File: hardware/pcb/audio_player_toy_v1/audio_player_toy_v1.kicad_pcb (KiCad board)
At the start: 2 copper layers, 70 x 50 mm, 14 parts, among them J1 Conn_02x05_Odd_Even, U1 ISD2360YYI, U2 BH-AAA-B5AA005

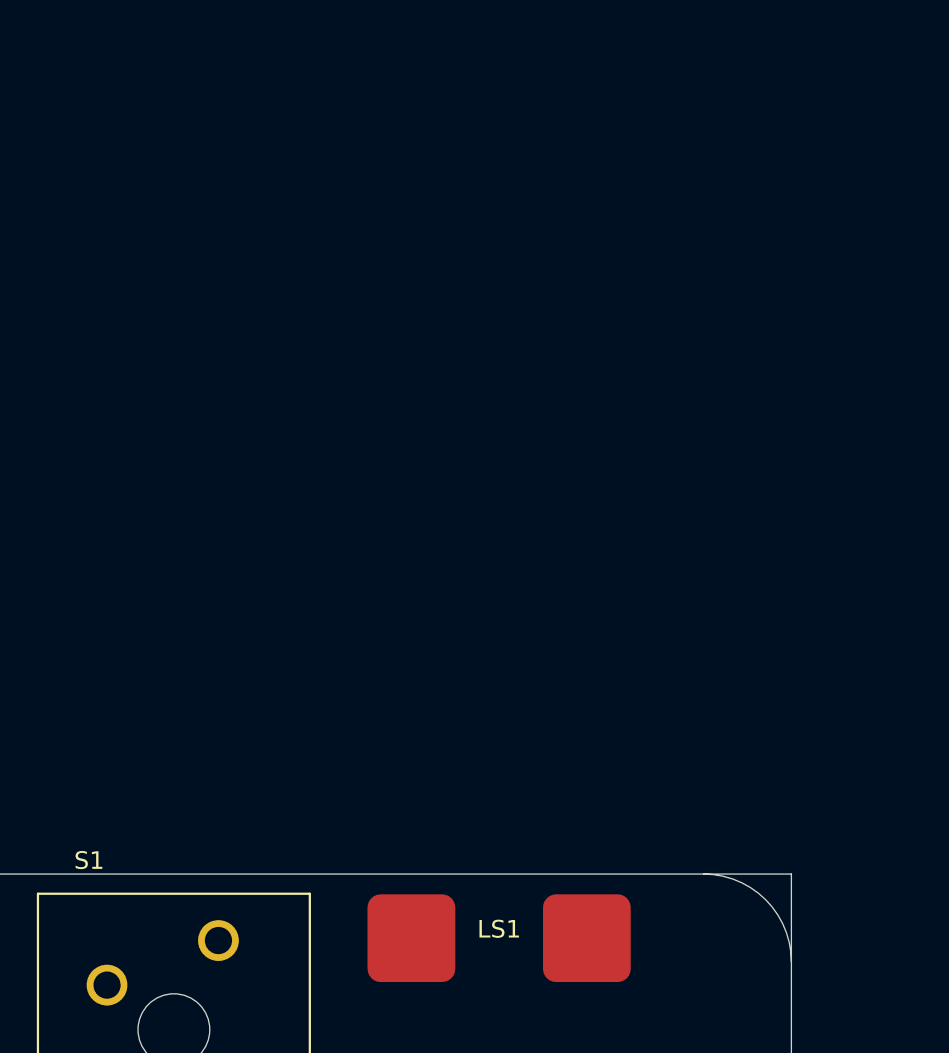
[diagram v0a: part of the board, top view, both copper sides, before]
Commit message: feat: add TH speaker capacbility
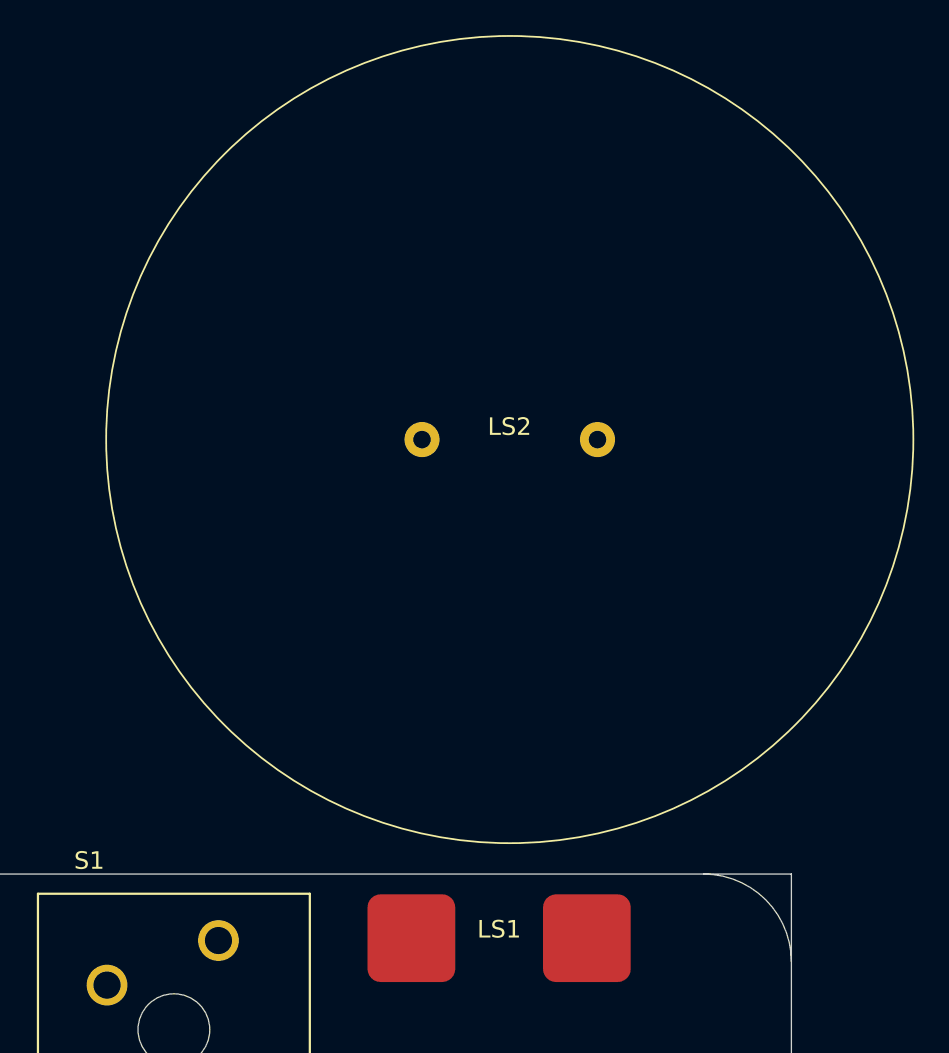
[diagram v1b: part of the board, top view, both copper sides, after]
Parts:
- added LS2: Speaker, .pretty:Speaker_TH, F.Cu at (153.9, 75.2)
- LS1: footprint .pretty:Speaker -> .pretty:Speaker_SMD
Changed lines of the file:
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@@
 		)
 	)
-	(footprint ".pretty:Speaker"
+	(footprint ".pretty:Speaker_SMD"
 		(layer "F.Cu")
 		(at 153.345 103.655)
 		(property "Reference" "LS1"
-			(at 0 -0.499999 0)
+			(at 0 -0.5 0)
 			(unlocked yes)
 			(layer "F.SilkS")
@@
 			(solder_mask_margin 0.102)
 		)
+		(embedded_fonts no)
+	)
+	(footprint ".pretty:Speaker_TH"
+		(layer "F.Cu")
+		(at 153.95 75.24)
+		(property "Reference" "LS2"
+			(at -0.01 -0.73 0)
+			(unlocked yes)
+			(layer "F.SilkS")
+			(effects
+				(font
+					(size 1 1)
+					(thickness 0.1)
+				)
+			)
+		)
+		(property "Value" "Speaker"
+			(at 0 1 0)
+			(unlocked yes)
+			(layer "F.Fab")
+			(effects
+				(font
+					(size 1 1)
+					(thickness 0.15)
+				)
+			)
+		)
+		(property "Datasheet" "~"
+			(at 0 0 0)
+			(unlocked yes)
+			(layer "F.Fab")
+			(hide yes)
+			(effects
+				(font
+					(size 1 1)
+					(thickness 0.15)
+				)
+			)
+		)
+		(property "Description" "Speaker"
+			(at 0 0 0)
+			(unlocked yes)
+			(layer "F.Fab")
+			(hide yes)
+			(effects
+				(font
+					(size 1 1)
+					(thickness 0.15)
+				)
+			)
+		)
+		(sheetname "/")
+		(sheetfile "audio_player_toy_v1.kicad_sch")
+		(attr smd)
+		(fp_circle
+			(center 0 0)
+			(end 23 0)
+			(stroke
+				(width 0.1)
+				(type solid)
+			)
+			(fill no)
+			(layer "F.SilkS")
+		)
+		(fp_circle
+			(center 0 0)
+			(end 23.5 0)
+			(stroke
+				(width 0.1)
+				(type solid)
+			)
+			(fill no)
+			(layer "F.CrtYd")
+		)
+		(fp_text user "${REFERENCE}"
+			(at 0 2.5 0)
+			(unlocked yes)
+			(layer "F.Fab")
+			(effects
+				(font
+					(size 1 1)
+					(thickness 0.15)
+				)
+			)
+		)
+		(pad "1" thru_hole circle
+			(at -5 0)
+			(size 2 2)
+			(drill 1)
+			(layers "*.Cu" "*.Mask")
+			(remove_unused_layers no)
+			(net 23 "SPK+")
+			(pinfunction "1")
+			(pintype "input")
+			(solder_mask_margin 0.102)
+		)
+		(pad "2" thru_hole circle
+			(at 5 0)
+			(size 2 2)
+			(drill 1)
+			(layers "*.Cu" "*.Mask")
+			(remove_unused_layers no)
+			(net 29 "SPK-")
+			(pinfunction "2")
+			(pintype "input")
+			(solder_mask_margin 0.102)
+		)

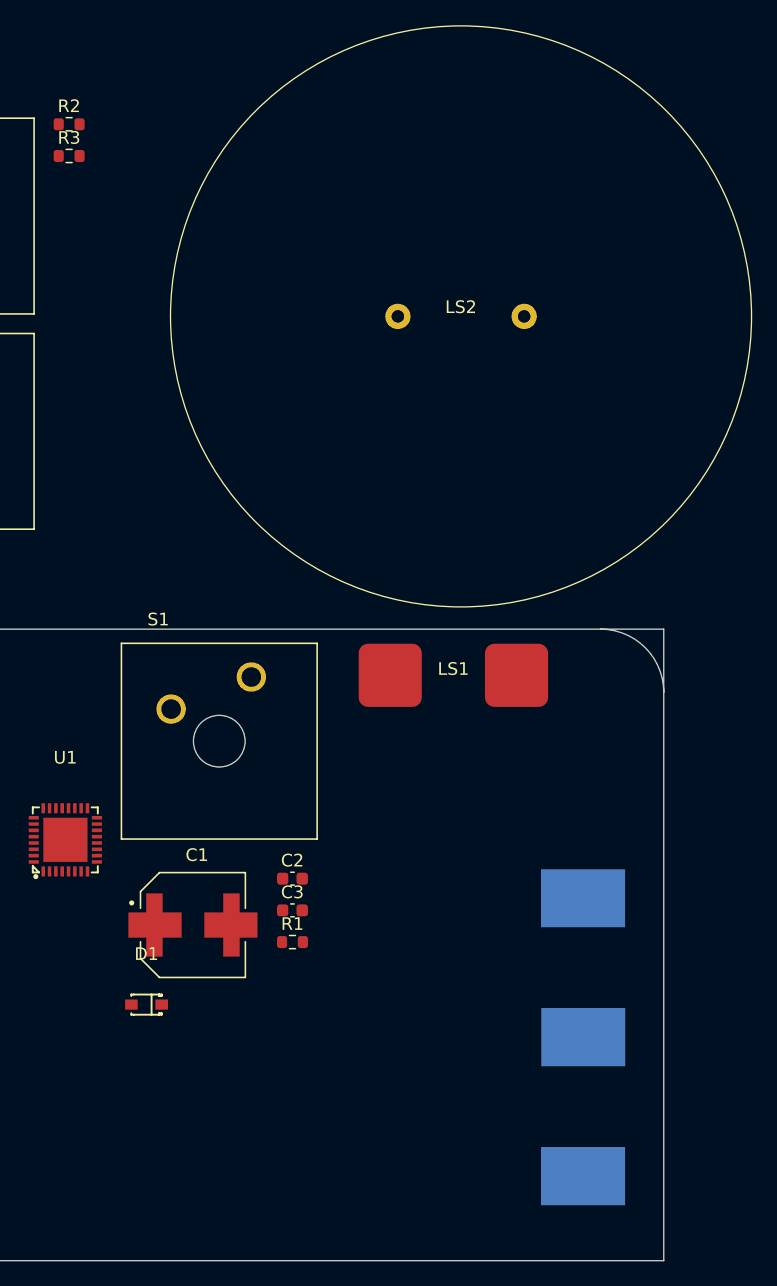
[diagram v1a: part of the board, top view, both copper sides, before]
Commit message: chore: update footprint of speaker TH
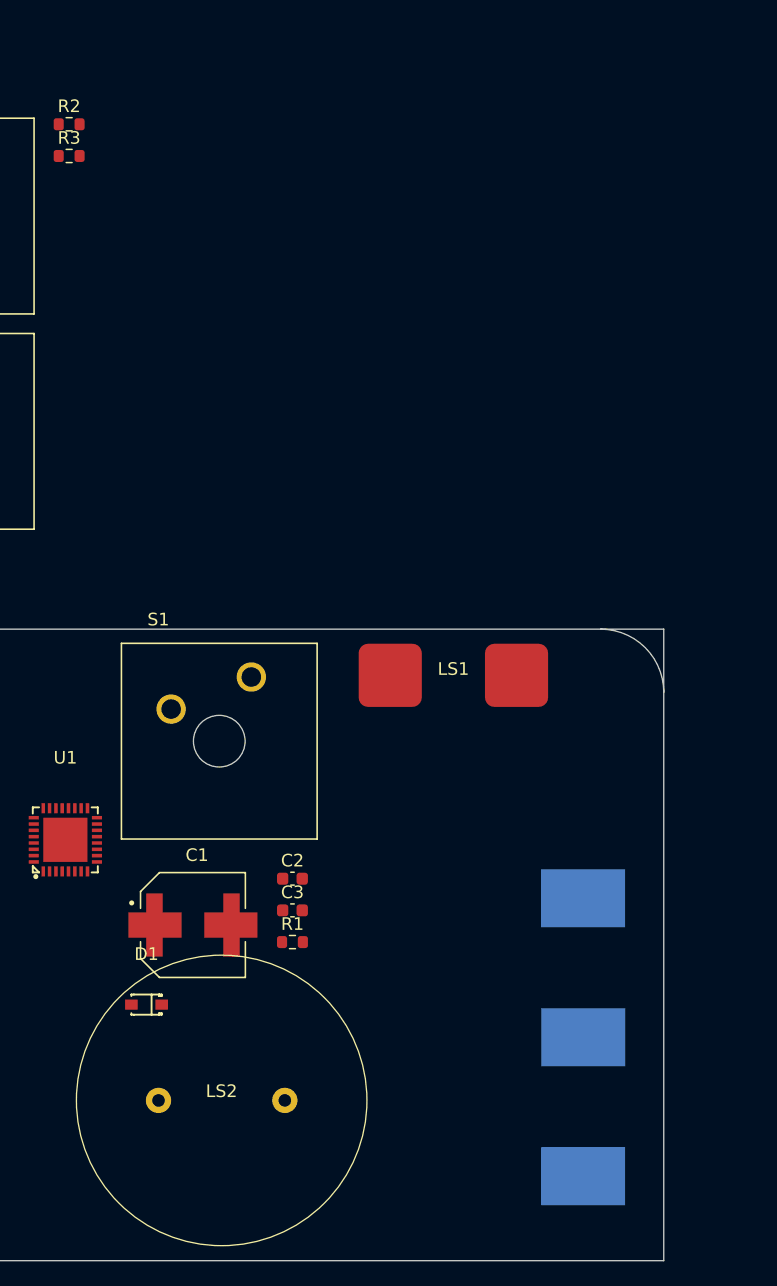
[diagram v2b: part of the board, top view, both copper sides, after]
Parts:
- moved LS2 64.9 mm to (135.0, 137.3)
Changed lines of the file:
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@@
 	(footprint ".pretty:Speaker_TH"
 		(layer "F.Cu")
-		(at 153.95 75.24)
+		(at 135 137.31)
 		(property "Reference" "LS2"
 			(at -0.01 -0.73 0)
@@
 		(fp_circle
 			(center 0 0)
-			(end 23 0)
+			(end 11.5 0)
 			(stroke
 				(width 0.1)
@@
 		(fp_circle
 			(center 0 0)
-			(end 23.5 0)
+			(end 12 0)
 			(stroke
 				(width 0.1)

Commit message: chore: finalize the location of main component
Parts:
- moved D1 60.2 mm to (79.2, 96.0)
- moved U1 60.2 mm to (72.8, 82.9)
- moved R1 60.2 mm to (90.8, 91.0)
- moved C1 60.2 mm to (82.9, 89.7)
- moved C2 60.2 mm to (90.8, 86.0)
- moved C3 60.2 mm to (90.8, 88.5)
- moved S2 50.5 mm to (135.0, 112.5)
- moved J1 37.7 mm to (135.2, 80.9)
- moved S3 28.3 mm to (115.0, 112.5)
- moved S1 20.5 mm to (155.0, 112.5)
- moved LS1 16.1 mm to (153.0, 87.5)
- moved U2 0.76 mm to (135.0, 132.0)
- moved LS2 0.63 mm to (135.0, 136.7)
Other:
- board size 70 x 50 mm -> 70 x 52.5 mm
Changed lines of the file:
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@@
 	(footprint "Capacitor_SMD:C_0603_1608Metric"
 		(layer "F.Cu")
-		(at 140.605 119.755)
+		(at 90.795 85.985)
 		(descr "Capacitor SMD 0603 (1608 Metric), square (rectangular) end terminal, IPC-7351 nominal, (Body size source: IPC-SM-782 page 76, https://www.pcb-3d.com/wordpress/wp-content/uploads/ipc-sm-782a_amendment_1_and_2.pdf), generated with kicad-footprint-generator")
 		(tags "capacitor")
@@
 	(footprint ".pretty:SOD-323_L1.8-W1.3-LS2.5-FD"
 		(layer "F.Cu")
-		(at 129.05 129.725)
+		(at 79.24 95.955)
 		(property "Reference" "D1"
 			(at 0 -4 0)
@@
 	(footprint "Capacitor_SMD:C_0603_1608Metric"
 		(layer "F.Cu")
-		(at 140.605 122.265)
+		(at 90.795 88.495)
 		(descr "Capacitor SMD 0603 (1608 Metric), square (rectangular) end terminal, IPC-7351 nominal, (Body size source: IPC-SM-782 page 76, https://www.pcb-3d.com/wordpress/wp-content/uploads/ipc-sm-782a_amendment_1_and_2.pdf), generated with kicad-footprint-generator")
 		(tags "capacitor")
@@
 	(footprint ".pretty:Speaker_SMD"
 		(layer "F.Cu")
-		(at 153.345 103.655)
+		(at 153 87.54)
 		(property "Reference" "LS1"
 			(at 0 -0.5 0)
@@
 	(footprint ".pretty:SW_MX1A-11NN"
 		(layer "F.Cu")
-		(at 134.81 108.87)
+		(at 155 112.5)
 		(property "Reference" "S1"
 			(at -4.822 -9.632 0)
@@
 	(footprint "Resistor_SMD:R_0603_1608Metric"
 		(layer "F.Cu")
-		(at 140.605 124.775)
+		(at 90.795 91.005)
 		(descr "Resistor SMD 0603 (1608 Metric), square (rectangular) end terminal, IPC-7351 nominal, (Body size source: IPC-SM-782 page 72, https://www.pcb-3d.com/wordpress/wp-content/uploads/ipc-sm-782a_amendment_1_and_2.pdf), generated with kicad-footprint-generator")
 		(tags "resistor")
@@
 	(footprint ".pretty:SW_MX1A-11NN"
 		(layer "F.Cu")
-		(at 112.4 67.296)
+		(at 135 112.5)
 		(property "Reference" "S2"
 			(at -4.822 -9.632 0)
@@
 	(footprint ".pretty:Speaker_TH"
 		(layer "F.Cu")
-		(at 135 137.31)
+		(at 135 136.675)
 		(property "Reference" "LS2"
 			(at -0.01 -0.73 0)
@@
 	(footprint ".pretty:CAP_EEEFK1A221V"
 		(layer "F.Cu")
-		(at 132.725 123.425)
+		(at 82.915 89.655)
 		(property "Reference" "C1"
 			(at 0.325 -5.535 0)
@@
 	(footprint ".pretty:TQFN-32_L5.0-W5.0-P0.50-BL-EP3.5"
 		(layer "F.Cu")
-		(at 122.625 116.68)
+		(at 72.815 82.91)
 		(property "Reference" "U1"
 			(at 0 -6.5 0)
@@
 	(footprint "Connector_PinHeader_2.54mm:PinHeader_2x05_P2.54mm_Vertical"
 		(layer "F.Cu")
-		(at 105.635 104.26)
+		(at 135.215 80.93)
 		(descr "Through hole straight pin header, 2x05, 2.54mm pitch, double rows")
 		(tags "Through hole pin header THT 2x05 2.54mm double row")
@@
 	(footprint ".pretty:SW_MX1A-11NN"
 		(layer "F.Cu")
-		(at 112.4 84.34)
+		(at 115 112.5)
 		(property "Reference" "S3"
 			(at -4.822 -9.632 0)
@@
 	(footprint ".pretty:BAT-SMD_BH-AAA-B5AA005"
 		(layer "B.Cu")
-		(at 135.695 132.305 180)
+		(at 135 132 180)
 		(property "Reference" "U2"
 			(at 0 15 0)
@@
 		)
 	)
-	(gr_arc
-		(start 165 100)
-		(mid 168.535534 101.464466)
-		(end 170 105)
+	(gr_rect
+		(start 117.42 131.175)
+		(end 152.42 142.175)
 		(stroke
-			(width 0.05)
-			(type default)
+			(width 0.1)
+			(type solid)
 		)
-		(layer "Edge.Cuts")
+		(fill no)
+		(layer "F.SilkS")
 	)
 	(gr_rect
 		(start 100 100)
-		(end 170 150)
+		(end 170 152.5)
 		(stroke
 			(width 0.05)

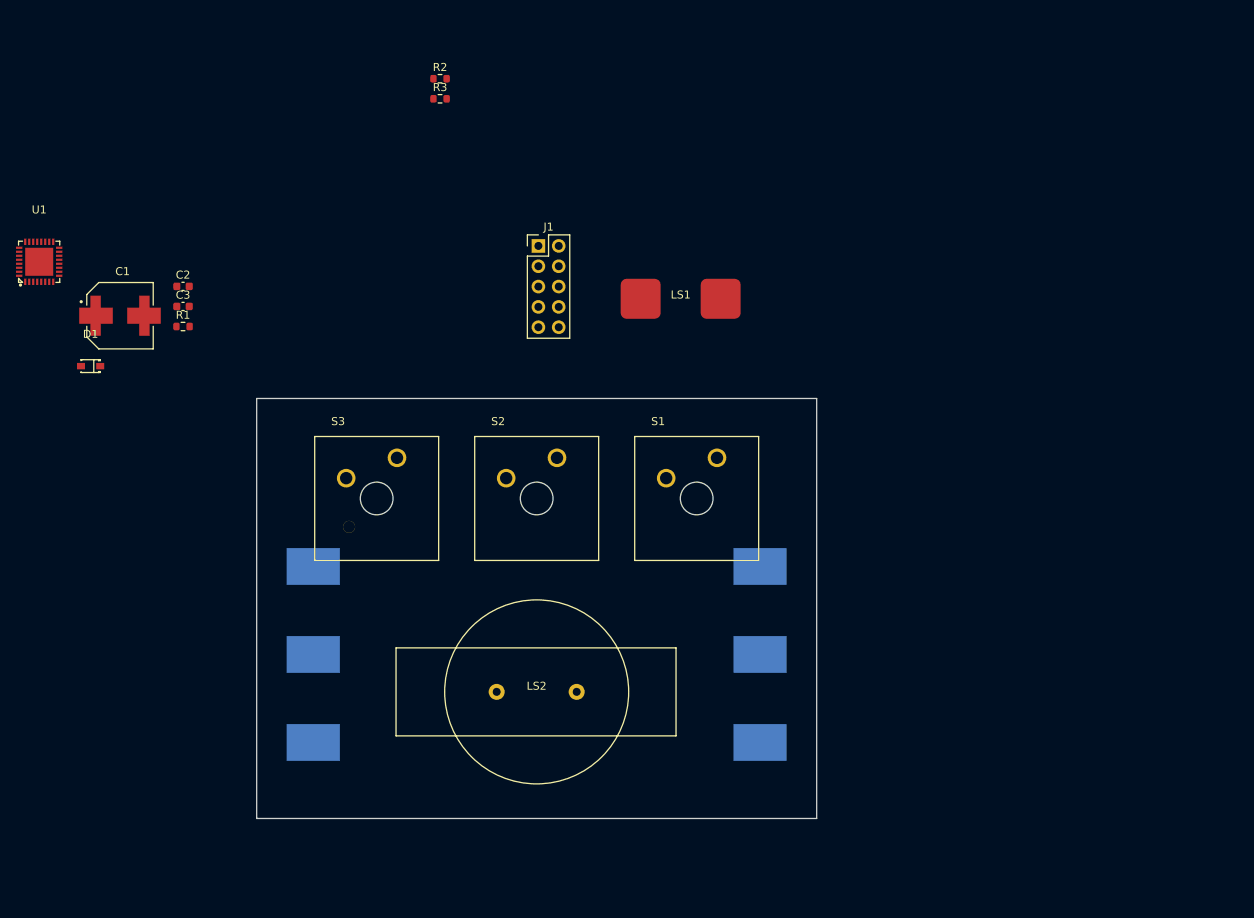
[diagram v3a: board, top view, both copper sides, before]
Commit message: chore: resize the pcb
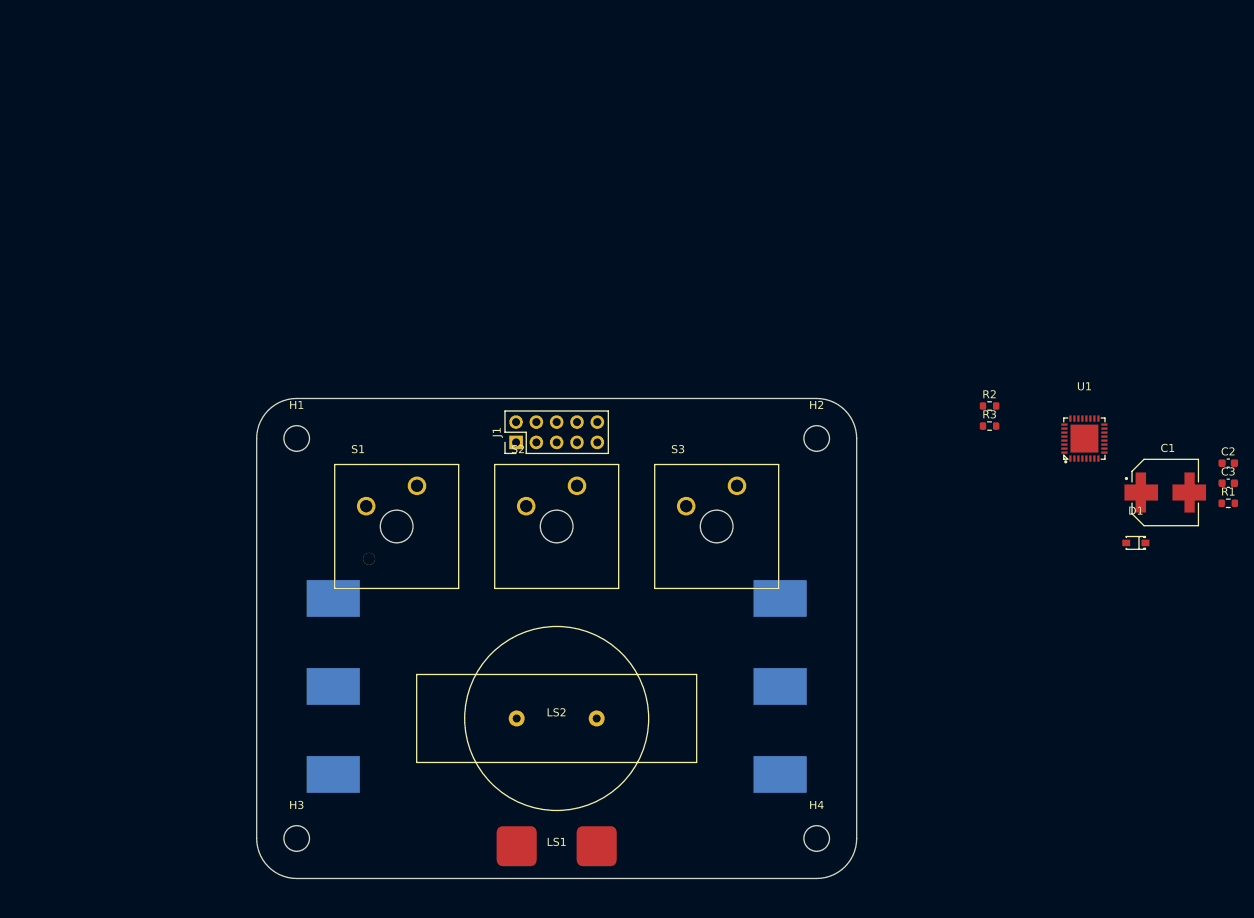
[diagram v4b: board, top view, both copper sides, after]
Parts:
- added H1: MountingHole, MountingHole:MountingHole_3.2mm_M3, F.Cu at (105.0, 105.0)
- added H2: MountingHole, MountingHole:MountingHole_3.2mm_M3, F.Cu at (170.0, 105.0)
- added H3: MountingHole, MountingHole:MountingHole_3.2mm_M3, F.Cu at (105.0, 155.0)
- added H4: MountingHole, MountingHole:MountingHole_3.2mm_M3, F.Cu at (170.0, 155.0)
- moved D1 132.5 mm to (209.9, 118.1)
- moved U1 132.5 mm to (203.5, 105.0)
- moved C1 132.5 mm to (213.6, 111.8)
- moved C2 132.5 mm to (221.4, 108.1)
- moved C3 132.5 mm to (221.4, 110.6)
- moved R1 132.5 mm to (221.4, 113.1)
- moved R3 79.9 mm to (191.6, 103.5)
- moved R2 79.9 mm to (191.6, 100.9)
- moved LS1 70.2 mm to (137.5, 156.0)
- moved S3 42.6 mm to (157.5, 116.0)
- moved S1 37.7 mm to (117.5, 116.0)
- moved J1 24.7 mm to (132.4, 105.5), turned to 90 degrees
- moved U2 4.72 mm to (137.5, 136.0)
- moved S2 4.30 mm to (137.5, 116.0)
- moved LS2 4.16 mm to (137.5, 140.0)
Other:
- board size 70 x 52.5 mm -> 75 x 60 mm

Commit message: feat: finish routing pcb
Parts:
- moved R1 110.8 mm to (111.4, 125.6), turned to 180 degrees
- moved C1 94.5 mm to (121.1, 131.5), turned to 90 degrees
- moved D1 94.0 mm to (118.9, 141.5), turned to 90 degrees
- moved C3 74.4 mm to (152.9, 139.5), turned to 180 degrees
- moved C2 65.4 mm to (160.0, 130.5)
- moved R2 63.7 mm to (132.9, 125.6)
- moved U1 55.9 mm to (156.2, 134.7), turned to -90 degrees
- moved R3 44.6 mm to (152.9, 125.6)
- moved J1 10.5 mm to (142.6, 103.0), turned to -90 degrees
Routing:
- net BAT+: track 0.00 -> 101.5 mm
- net RDY/BSYB: track 0.00 -> 94.4 mm
- net INTB: track 0.00 -> 80.9 mm, vias 0 -> 2
- net MOSI: track 0.00 -> 42.5 mm, vias 0 -> 1
- net SPK+: track 0.00 -> 41.9 mm, vias 0 -> 1
- net SCLK: track 0.00 -> 41.8 mm, vias 0 -> 2
- net SPK-: track 0.00 -> 41.8 mm, vias 0 -> 1
- net MISO: track 0.00 -> 38.2 mm, vias 0 -> 2
- net SSB: track 0.00 -> 32.9 mm, vias 0 -> 1
- net GPIO5: track 0.00 -> 32.3 mm, vias 0 -> 1
- net GND: track 0.00 -> 7.81 mm, vias 0 -> 1
- net Net-(D1-A): vias 0 -> 4
- added copper zone on F.Cu, net BAT+
- added copper zone on B.Cu, net GND
- added copper zone on F.Cu, net GND
- added copper zone on B.Cu, net Net-(D1-A)
- added copper zone on F.Cu, net Net-(D1-A)
- added copper zone on B.Cu, net Net-(U2-+-Pad2)
- added copper zone on B.Cu, net Net-(U2-+-Pad6)
